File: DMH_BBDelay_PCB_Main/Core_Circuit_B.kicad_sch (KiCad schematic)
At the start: 76 parts, among them J30 Conn_01x08, J31 Conn_01x08, J32 Conn_01x08, J33 Conn_01x08, Q8 J113, SW1 SW_DPDT_3way_x2, SW2 SW_DPDT_x2, SW4 SW_SPDT, U18 CD4053B, U5 TL074, U6 TL074, U7 V3205, U8 CD4046, U9 40106

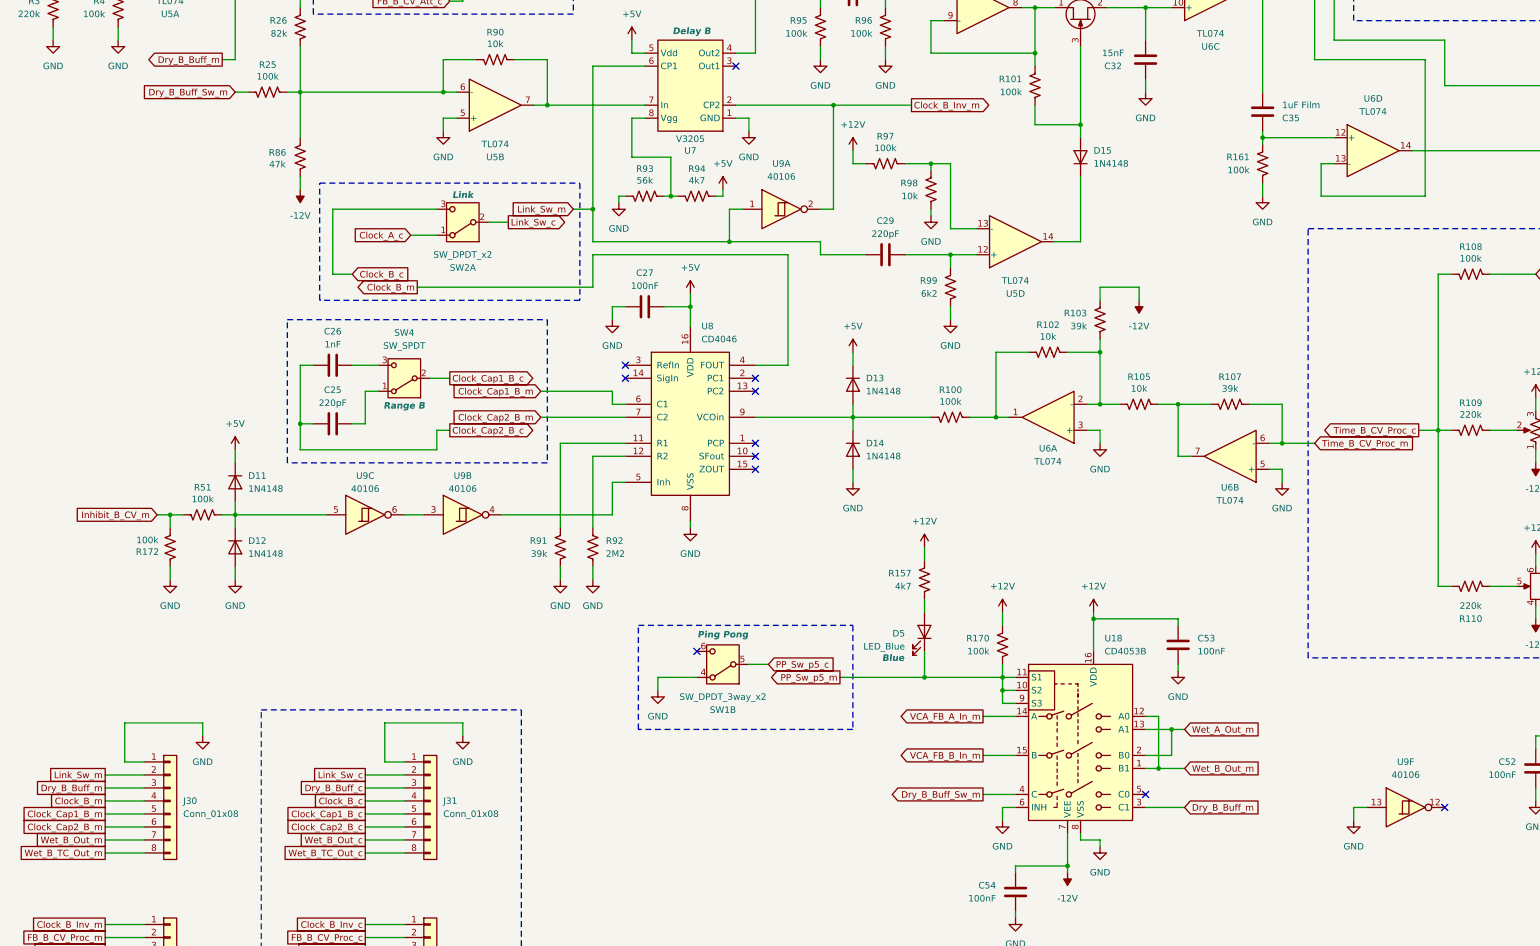
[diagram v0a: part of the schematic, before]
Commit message: Fixed linking function
Used idle 40106 gate to buffer clock A before injecting it into V3205 B
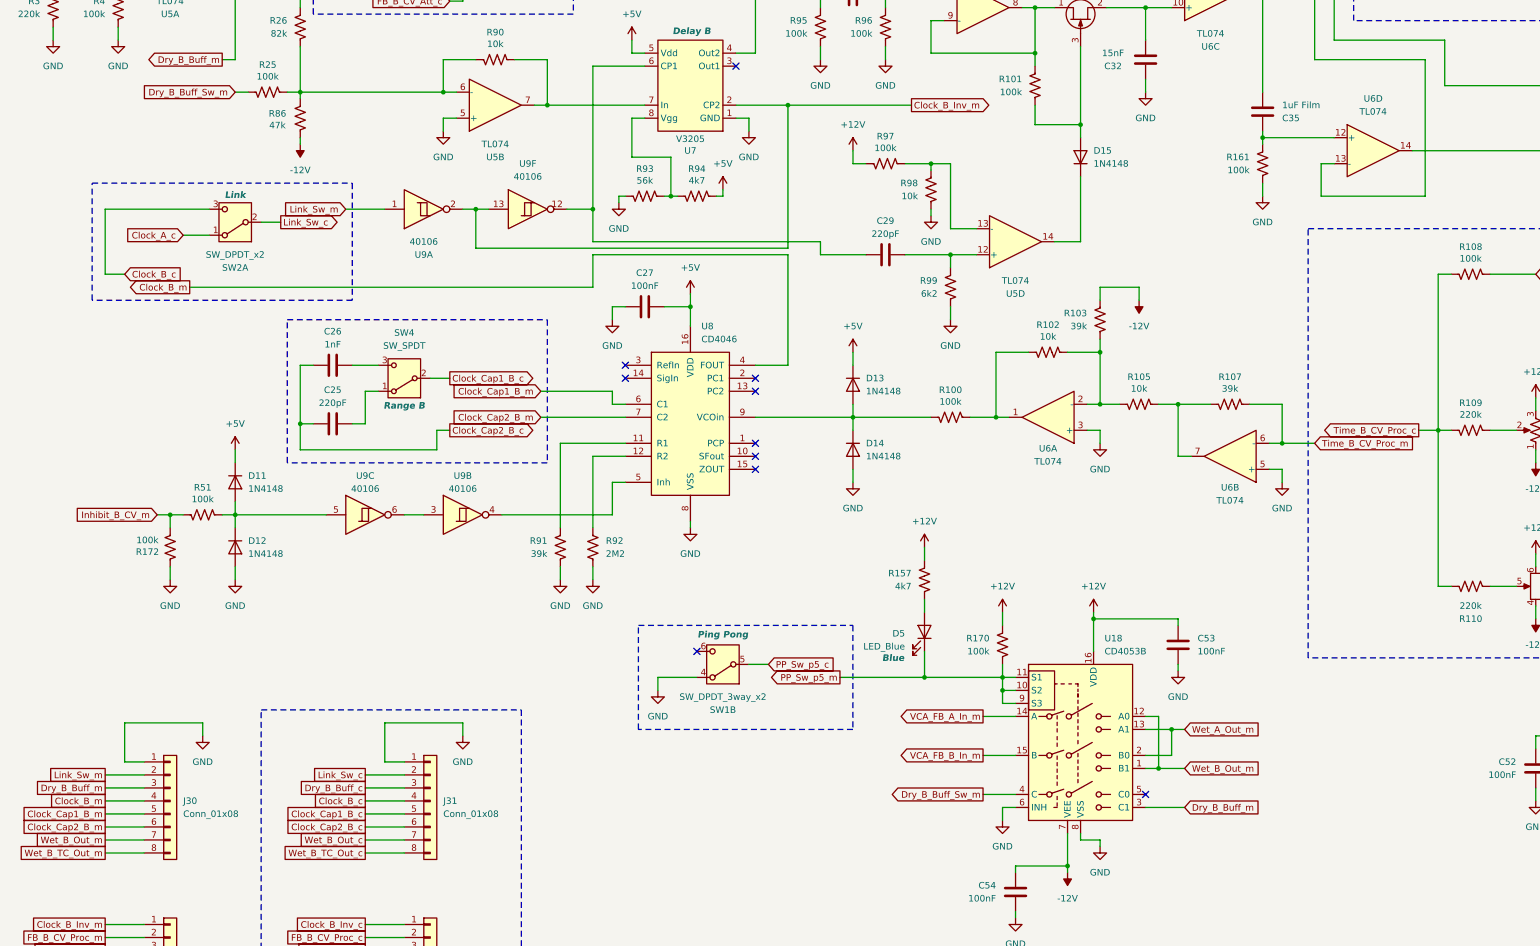
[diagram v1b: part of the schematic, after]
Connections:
- net Clock_B_Inv_m: now also U9.13
- net GND: no longer U9.13
- net Link_Sw_m: no longer C29.1, U7.6 (CP1)
- net at U9.12: now also C29.1, U7.6 (CP1)
- no-connect marks 13 -> 12
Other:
- moved on the sheet: R86, SW2A

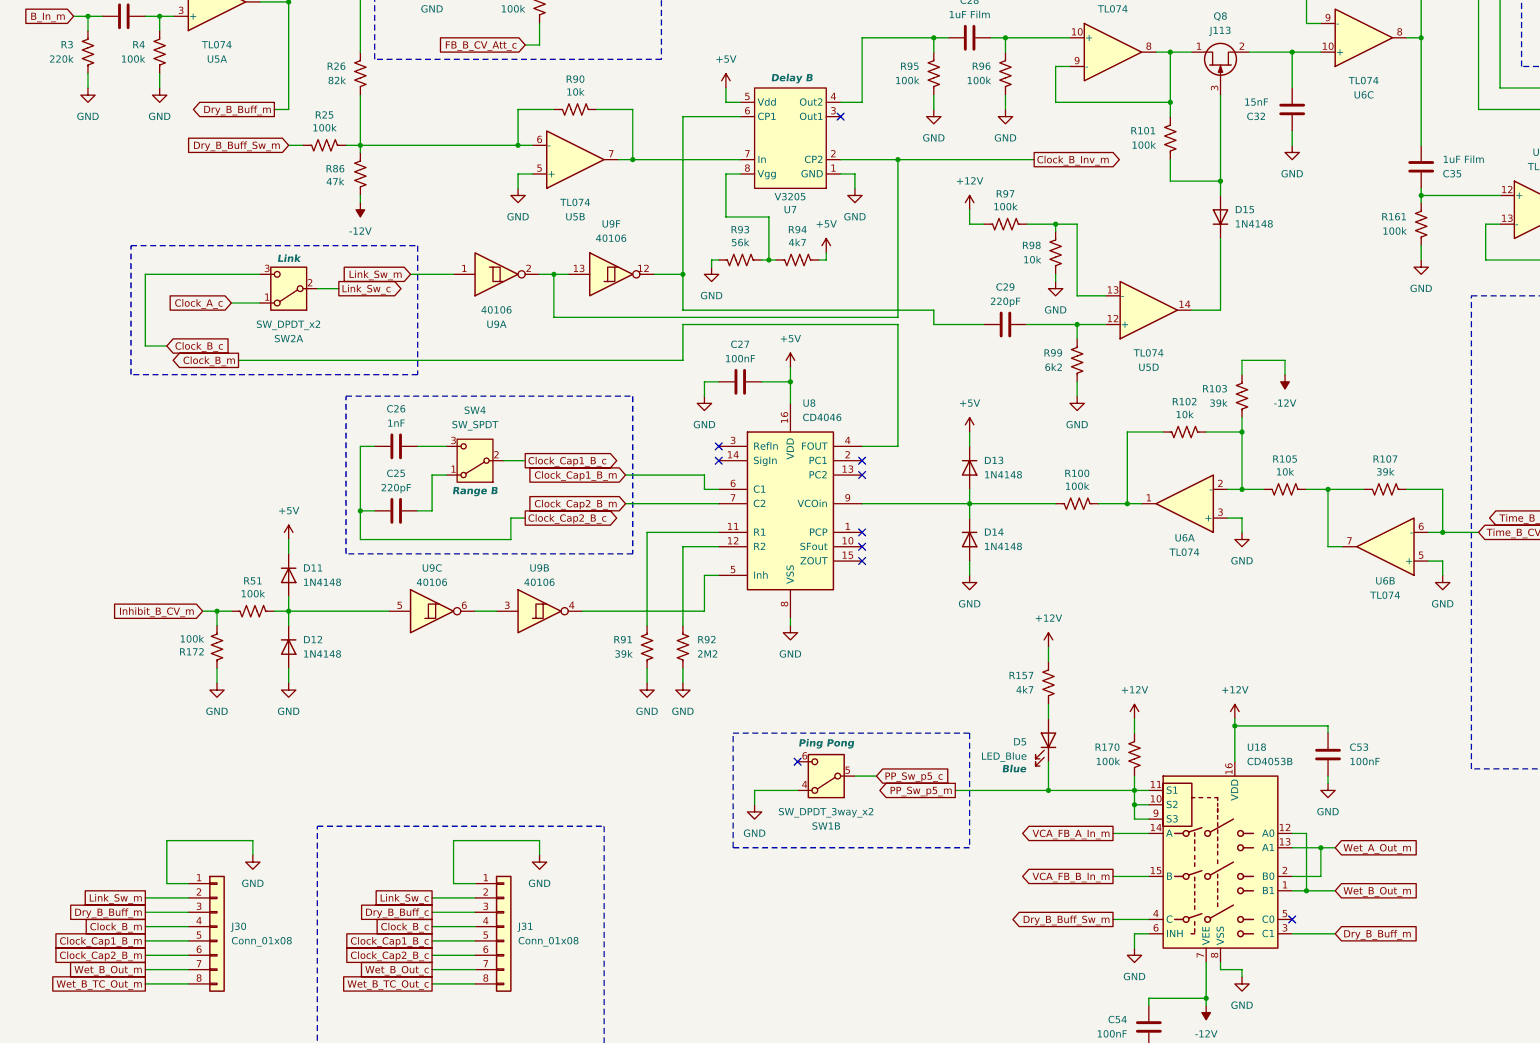
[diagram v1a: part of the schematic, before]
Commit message: Added input filters
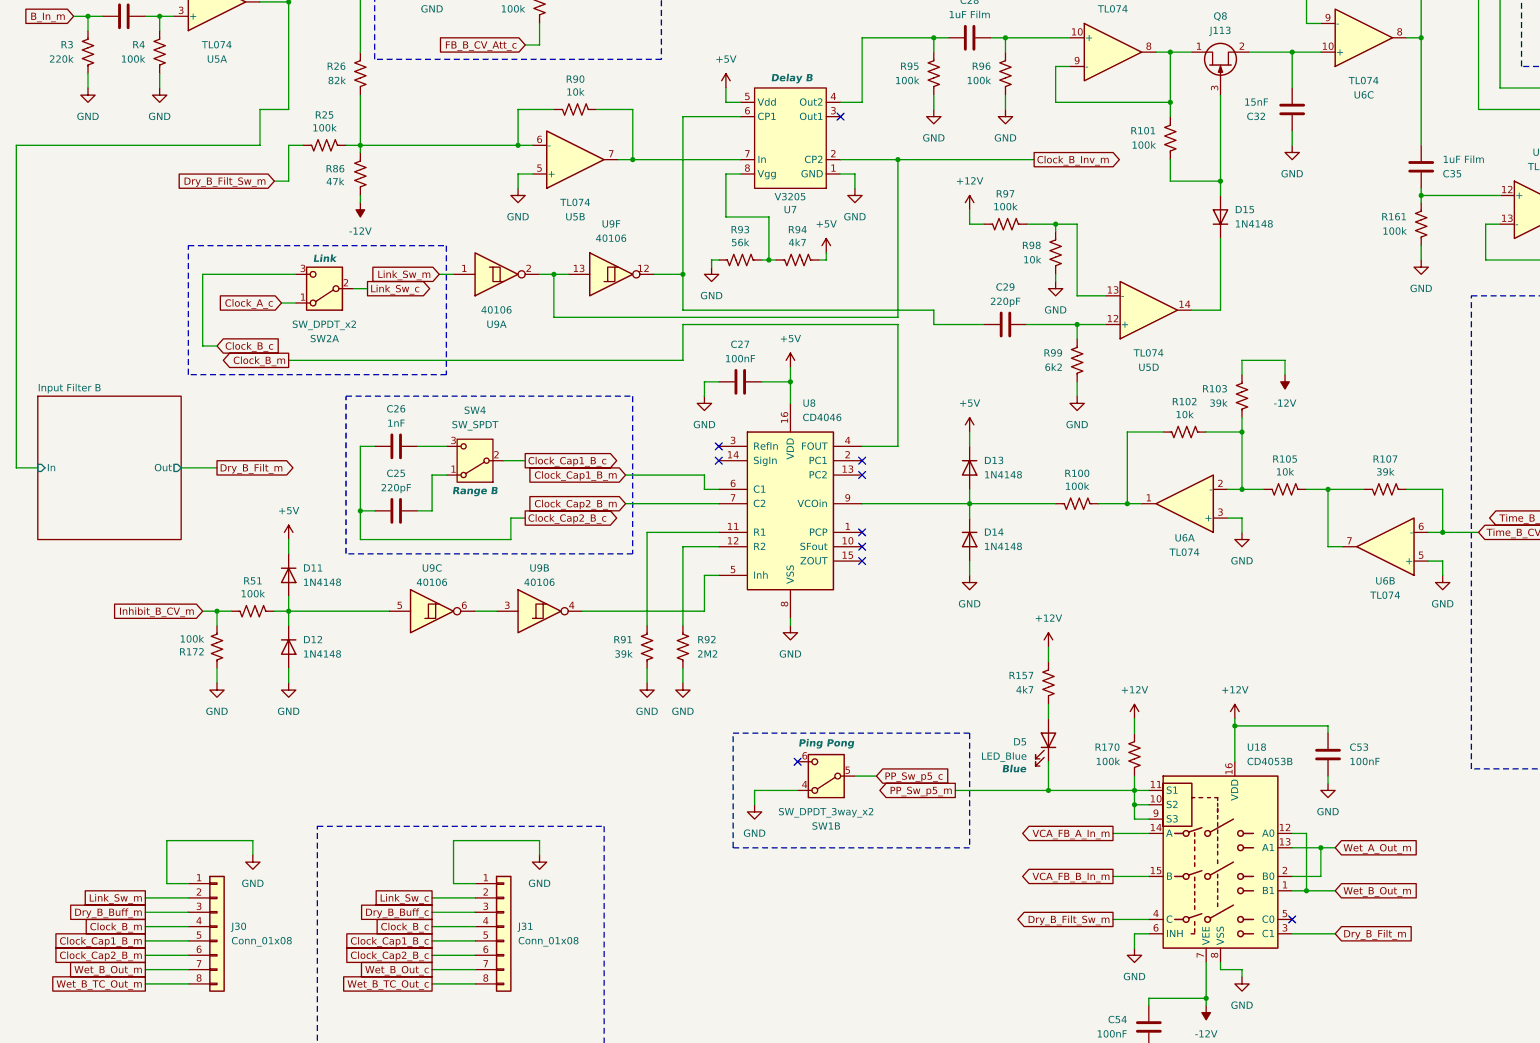
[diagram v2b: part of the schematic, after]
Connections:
- net Dry_B_Buff_m: no longer U18.3 (C1)
- net Dry_B_Buff_Sw_m renamed Dry_B_Filt_Sw_m
- new net Dry_B_Filt_m: U18.3 (C1)
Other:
- added sheet Input Filter B (Input_Filter_B.kicad_sch)
- moved on the sheet: SW2A
